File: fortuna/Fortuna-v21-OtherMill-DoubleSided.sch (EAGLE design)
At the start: 41 parts, among them J1 5V, J2 GND, J3 A0, J4 A3, J5 A5, J6 D2, J7 *D5, J8 *D10, J9 VIN, M1 MOTOR20MM, M2 MOTOR20MM, Q1 PN2222A, Q2 PN2222A, U1 OPA2344, U2 OPA2344

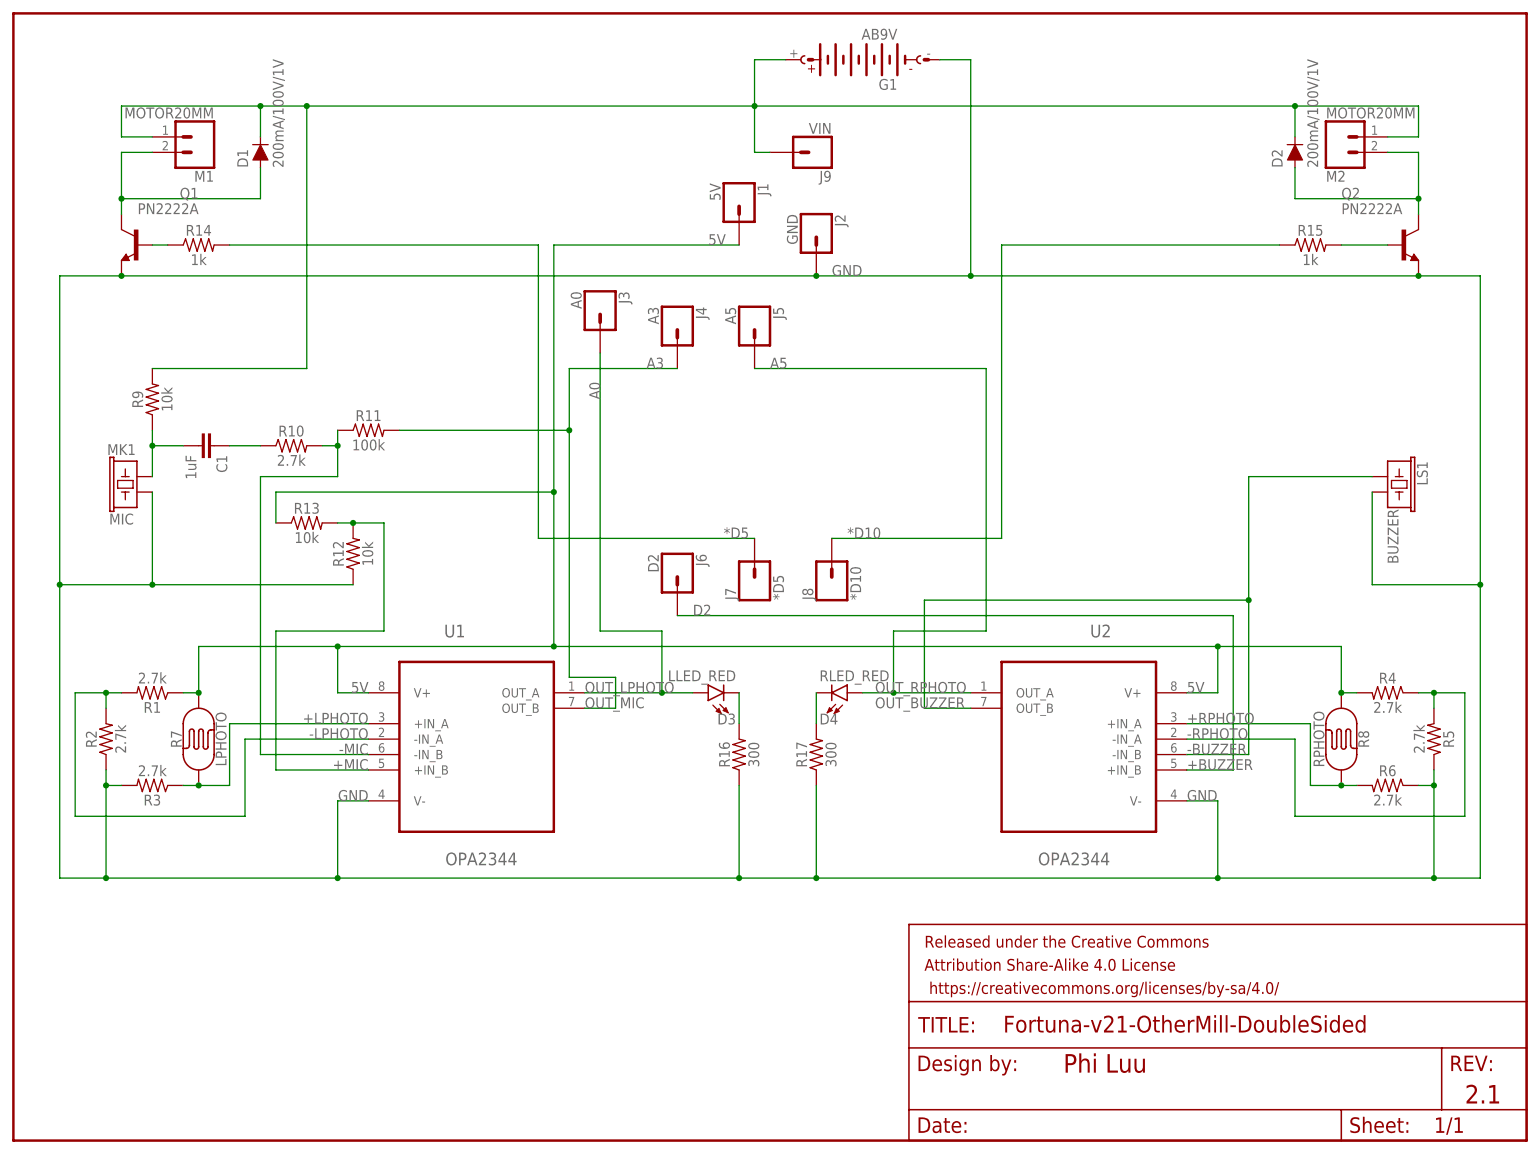
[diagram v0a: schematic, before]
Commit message: Merge two OPA2344's into one OPA4344 & Add SPDT power switch
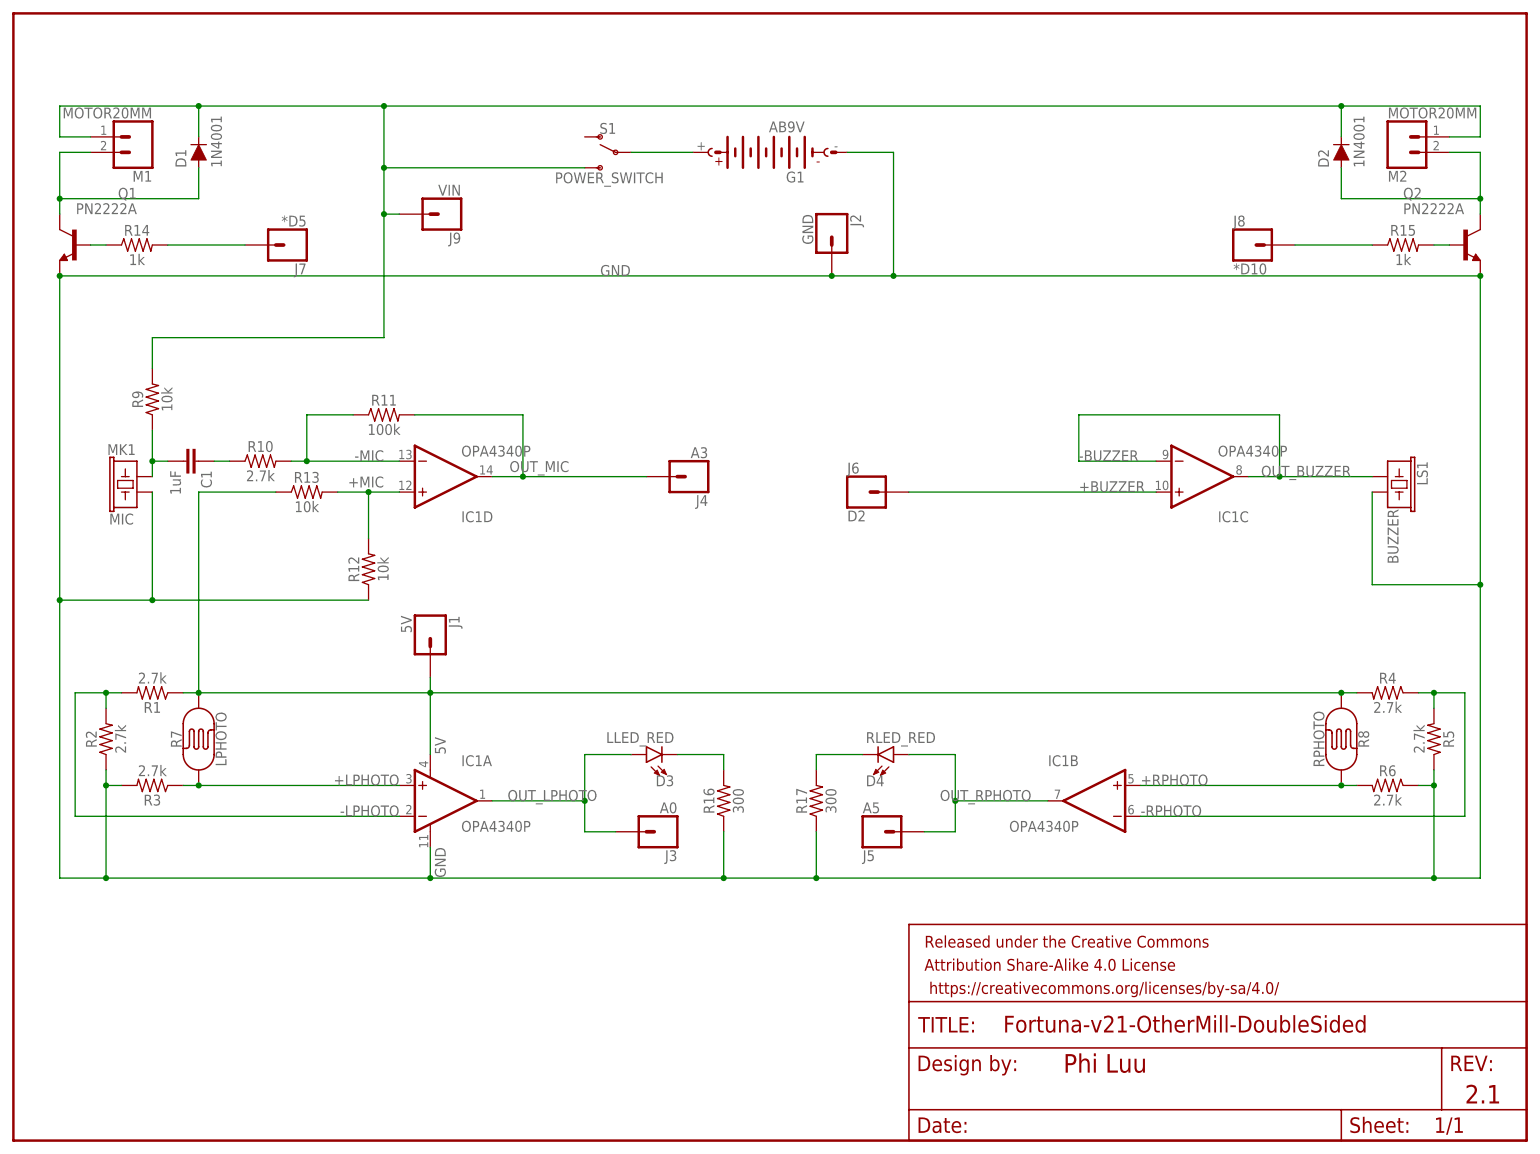
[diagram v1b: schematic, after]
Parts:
- removed U1, U2: OPA2344, TexasInstruments:OPA2277PA
- added IC1: OPA4340P, burr-brown:OPA4340P
- added S1: POWER_SWITCH, SparkFun-Switches:SWITCH-SPDT-PTH-11.6X4.0MM
- D1, D2: value 200mA/100V/1V -> 1N4001
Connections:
- net *D10 renamed OUT_RMOTOR
- net *D5 renamed OUT_LMOTOR
- removed net A0: D3.A, J3.1, U1.OUT_A
- removed net A3: J4.1, R11.2, U1.OUT_B
- removed net A5: D4.A, J5.1, U2.OUT_A
- new net 9V: G1.+, S1.P
- new net OUT_LPHOTO: D3.A, IC1A.OUT, J3.1
- new net OUT_MIC: IC1D.OUT, J4.1, R11.2
- new net OUT_RPHOTO: D4.A, IC1B.OUT, J5.1
- net +LPHOTO: now also IC1A.+IN; no longer U1.+IN_A
- net +MIC: now also IC1D.+IN; no longer U1.+IN_B
- net +RPHOTO: now also IC1B.+IN; no longer U2.+IN_A
- net -LPHOTO: now also IC1A.-IN; no longer U1.-IN_A
- net -MIC: now also IC1D.-IN; no longer U1.-IN_B
- net -RPHOTO: now also IC1B.-IN; no longer U2.-IN_A
- net 5V: now also IC1A.V+; no longer U1.V+, U2.V+
- net D2: now also IC1C.+IN; no longer U2.+IN_B
- net GND: now also IC1A.V-; no longer U1.V-, U2.V-
- net OUT_BUZZER: now also IC1C.-IN, IC1C.OUT; no longer U2.-IN_B, U2.OUT_B
- net VIN: now also S1.S; no longer G1.+
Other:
- note removed: "OUT_LPHOTO"
- note removed: "OUT_MIC"
- note removed: "OUT_RPHOTO"
- moved on the sheet: C1, D1, D2, D3, D4, G1, J1, J2, J3, J4, J5, J6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

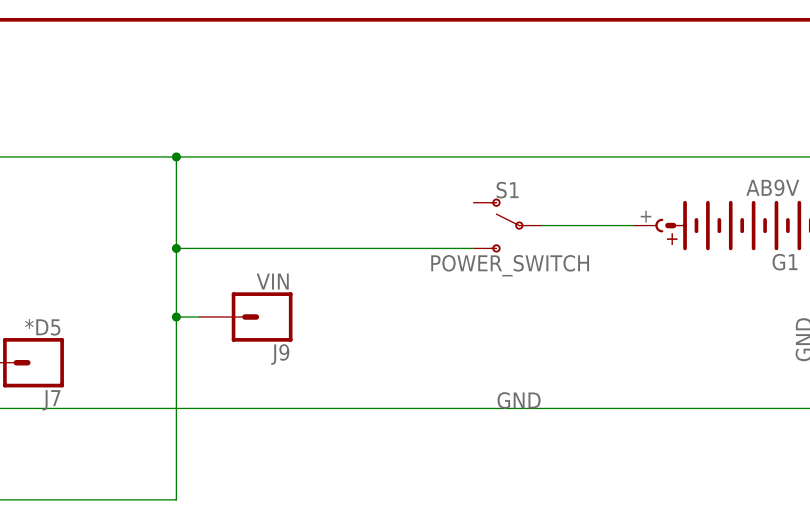
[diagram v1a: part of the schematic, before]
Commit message: Change pin position SPDT slide switch
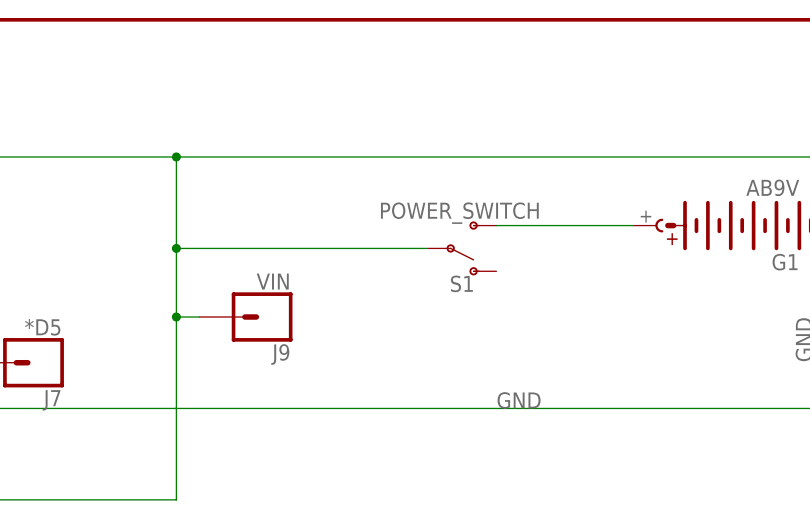
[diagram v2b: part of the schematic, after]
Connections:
- net 9V: now also S1.S; no longer S1.P
- net VIN: now also S1.P; no longer S1.S
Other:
- moved on the sheet: S1
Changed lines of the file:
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@@
 <setting verticaltext="up"/>
 </settings>
-<grid distance="0.1" unitdist="inch" unit="inch" style="lines" multiple="1" display="yes" altdistance="0.01" altunitdist="inch" altunit="inch"/>
+<grid distance="0.1" unitdist="inch" unit="inch" style="lines" multiple="1" display="no" altdistance="0.01" altunitdist="inch" altunit="inch"/>
 <layers>
 <layer number="1" name="Top" color="4" fill="1" visible="no" active="no"/>
@@
 <instance part="IC1" gate="C" x="195.58" y="109.22" rot="MR180"/>
 <instance part="IC1" gate="D" x="71.12" y="109.22" rot="MR180"/>
-<instance part="S1" gate="1" x="99.06" y="162.56" rot="MR0"/>
+<instance part="S1" gate="1" x="91.44" y="160.02" rot="MR180"/>
 </instances>
 <busses>
@@
 <wire x1="60.96" y1="132.08" x2="60.96" y2="152.4" width="0.1524" layer="91"/>
 <wire x1="60.96" y1="152.4" x2="60.96" y2="160.02" width="0.1524" layer="91"/>
-<wire x1="60.96" y1="160.02" x2="93.98" y2="160.02" width="0.1524" layer="91"/>
-<pinref part="S1" gate="1" pin="S"/>
-<wire x1="60.96" y1="160.02" x2="60.96" y2="170.18" width="0.1524" layer="91"/>
-<junction x="60.96" y="160.02"/>
 <junction x="60.96" y="170.18"/>
 <pinref part="J9" gate="G$1" pin="1"/>
+<wire x1="60.96" y1="160.02" x2="60.96" y2="170.18" width="0.1524" layer="91"/>
 <wire x1="60.96" y1="152.4" x2="63.5" y2="152.4" width="0.1524" layer="91"/>
 <junction x="60.96" y="152.4"/>
+<pinref part="S1" gate="1" pin="P"/>
+<wire x1="88.9" y1="160.02" x2="60.96" y2="160.02" width="0.1524" layer="91"/>
+<junction x="60.96" y="160.02"/>
 </segment>
 </net>
@@
 </segment>
 </net>
-<net name="9V" class="1">
+<net name="9V" class="0">
 <segment>
 <pinref part="G1" gate="G$1" pin="+"/>
-<pinref part="S1" gate="1" pin="P"/>
-<wire x1="111.76" y1="162.56" x2="101.6" y2="162.56" width="0.1524" layer="91"/>
-</segment>
-</net>
+<pinref part="S1" gate="1" pin="S"/>
+<wire x1="111.76" y1="162.56" x2="96.52" y2="162.56" width="0.1524" layer="91"/>
+</segment>
+</net>
